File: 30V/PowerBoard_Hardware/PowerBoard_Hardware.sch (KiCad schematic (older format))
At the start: 141 parts, among them Q1 Q_NMOS_GDS, Q10 Q_NMOS_GDS, Q2 Q_NMOS_GDS, Q3 Q_NMOS_GDS, Q4 Q_NMOS_GDS, Q5 Q_NMOS_GDS, Q6 Q_NMOS_GDS, Q7 Q_NMOS_GDS, Q8 Q_NMOS_GDS, Q9 Q_NMOS_GDS, U1 LT1910, U10 LT1910, U11 LT1910, U12 ACS722xLCTR-40AU, U13 ACS722xLCTR-40AU, U14 ACS722xLCTR-40AU, U15 OKI_5V, U16 OKI_3V3, U17 LT1910, U18 LT1910, U19 ACS722xLCTR-40AU, U2 LT1910, U20 ACS722xLCTR-40AU, U21 LT1910, U22 ACS722xLCTR-40AU, U3 LT1910, U4 LT1910, U5 ACS722xLCTR-40AU, U6 ACS722xLCTR-40AU, U7 ACS722xLCTR-40AU, U8 ACS722xLCTR-40AU, U9 LT1910

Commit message: redid PVDD
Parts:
- ConnTIVA_L1, ConnTIVA_R1: footprint Connector_PinHeader_1.27mm:PinHeader_2x05_P1.27mm_Vertical -> MRDT_Connectors:JTAG_ARM_Connector_10_Pin
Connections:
- net GND: now also C22.2, C25.2, C26.2, C27.2, D1.2 (A), D2.2 (A)
- net PVDD: now also C22.1, C25.1, C26.1, C27.1, D1.1 (K), D2.1 (K), V1.1; no longer C22.2, C25.2, C26.2, C27.2, D1.2 (A), D2.2 (A)
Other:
- note added: "12V_Board"
- moved on the sheet: C22, C25, C26, C27, D1, D2
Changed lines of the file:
@@
 Wire Wire Line
 	5450 5150 5450 5300
-Text GLabel 2700 4350 2    50   Output ~ 0
+Text GLabel 2700 3950 1    50   Output ~ 0
 PVDD
 Text GLabel 4750 850  0    50   Input ~ 0
@@
 F 0 "ConnTIVA_L1" H 1550 1550 60  0000 L CNN
 F 1 "PH_2x05" H 1650 1450 60  0000 L CNN
-F 2 "Connector_PinHeader_1.27mm:PinHeader_2x05_P1.27mm_Vertical" H 1800 1400 60  0001 C CNN
+F 2 "MRDT_Connectors:JTAG_ARM_Connector_10_Pin" H 1800 1400 60  0001 C CNN
 F 3 "" H 1800 1400 60  0001 C CNN
 	1    1800 1100
@@
 U 1 1 5E0EEBAD
 P 1700 2950
-F 0 "ConnTIVA_PWR1" H 1828 3208 60  0000 L CNN
+F 0 "ConnTIVA_PWR1" H 1850 3000 60  0000 L CNN
 F 1 "Molex_SL_02" H 1828 3102 60  0000 L CNN
 F 2 "MRDT_Connectors:MOLEX_SL_02_Vertical" H 1700 2950 60  0001 C CNN
@@
 L Device:CP1_Small C22
 U 1 1 5E7C9F9E
-P 750 4250
-F 0 "C22" H 838 4296 50  0000 L CNN
-F 1 "470uF" H 838 4205 50  0000 L CNN
-F 2 "Capacitor_THT:CP_Radial_D12.5mm_P5.00mm" H 750 4250 50  0001 C CNN
-F 3 "~" H 750 4250 50  0001 C CNN
-	1    750  4250
+P 750 4150
+F 0 "C22" H 838 4196 50  0000 L CNN
+F 1 "470uF" H 838 4105 50  0000 L CNN
+F 2 "Capacitor_THT:CP_Radial_D12.5mm_P5.00mm" H 750 4150 50  0001 C CNN
+F 3 "~" H 750 4150 50  0001 C CNN
+	1    750  4150
 	1    0    0    -1
 $EndComp
@@
 L Device:CP1_Small C25
 U 1 1 5E808371
-P 1100 4250
-F 0 "C25" H 1188 4296 50  0000 L CNN
-F 1 "470uF" H 1188 4205 50  0000 L CNN
-F 2 "Capacitor_THT:CP_Radial_D12.5mm_P5.00mm" H 1100 4250 50  0001 C CNN
-F 3 "~" H 1100 4250 50  0001 C CNN
-	1    1100 4250
+P 1100 4150
+F 0 "C25" H 1188 4196 50  0000 L CNN
+F 1 "470uF" H 1188 4105 50  0000 L CNN
+F 2 "Capacitor_THT:CP_Radial_D12.5mm_P5.00mm" H 1100 4150 50  0001 C CNN
+F 3 "~" H 1100 4150 50  0001 C CNN
+	1    1100 4150
 	1    0    0    -1
 $EndComp
@@
 L Device:CP1_Small C26
 U 1 1 5E808517
-P 1450 4250
-F 0 "C26" H 1538 4296 50  0000 L CNN
-F 1 "470uF" H 1538 4205 50  0000 L CNN
-F 2 "Capacitor_THT:CP_Radial_D12.5mm_P5.00mm" H 1450 4250 50  0001 C CNN
-F 3 "~" H 1450 4250 50  0001 C CNN
-	1    1450 4250
+P 1450 4150
+F 0 "C26" H 1538 4196 50  0000 L CNN
+F 1 "470uF" H 1538 4105 50  0000 L CNN
+F 2 "Capacitor_THT:CP_Radial_D12.5mm_P5.00mm" H 1450 4150 50  0001 C CNN
+F 3 "~" H 1450 4150 50  0001 C CNN
+	1    1450 4150
 	1    0    0    -1
 $EndComp
@@
 L Device:CP1_Small C27
 U 1 1 5E808A8A
-P 1800 4250
-F 0 "C27" H 1888 4296 50  0000 L CNN
-F 1 "470uF" H 1888 4205 50  0000 L CNN
-F 2 "Capacitor_THT:CP_Radial_D12.5mm_P5.00mm" H 1800 4250 50  0001 C CNN
-F 3 "~" H 1800 4250 50  0001 C CNN
-	1    1800 4250
-	1    0    0    -1
-$EndComp
-Wire Wire Line
-	750  4350 1100 4350
-Connection ~ 1100 4350
-Wire Wire Line
-	1100 4350 1450 4350
-Connection ~ 1450 4350
-Wire Wire Line
-	1450 4350 1800 4350
-Connection ~ 1800 4350
-Wire Wire Line
-	1800 4350 2100 4350
+P 1800 4150
+F 0 "C27" H 1888 4196 50  0000 L CNN
+F 1 "470uF" H 1888 4105 50  0000 L CNN
+F 2 "Capacitor_THT:CP_Radial_D12.5mm_P5.00mm" H 1800 4150 50  0001 C CNN
+F 3 "~" H 1800 4150 50  0001 C CNN
+	1    1800 4150
+	1    0    0    -1
+$EndComp
 $Comp
 L Device:D D1
 U 1 1 5E901D4D
-P 2100 4200
-F 0 "D1" V 2054 4279 50  0000 L CNN
-F 1 "1.5KE36A" V 2145 4279 50  0000 L CNN
-F 2 "Diode_THT:D_DO-201AD_P5.08mm_Vertical_KathodeUp" H 2100 4200 50  0001 C CNN
-F 3 "~" H 2100 4200 50  0001 C CNN
-	1    2100 4200
+P 2100 4150
+F 0 "D1" V 2054 4229 50  0000 L CNN
+F 1 "1.5KE36A" V 2145 4229 50  0000 L CNN
+F 2 "Diode_THT:D_DO-201AD_P5.08mm_Vertical_KathodeUp" H 2100 4150 50  0001 C CNN
+F 3 "~" H 2100 4150 50  0001 C CNN
+	1    2100 4150
 	0    1    1    0
 $EndComp
 Wire Wire Line
-	2600 4050 2600 4000
-Wire Wire Line
 	650  4000 750  4000
-Wire Wire Line
-	2100 4050 2100 4000
-Wire Wire Line
-	1800 4150 1800 4000
-Connection ~ 1800 4000
-Wire Wire Line
-	1800 4000 2100 4000
-Wire Wire Line
-	1450 4150 1450 4000
 Connection ~ 1450 4000
-Wire Wire Line
-	1450 4000 1800 4000
-Wire Wire Line
-	1100 4150 1100 4000
-Connection ~ 1100 4000
-Wire Wire Line
-	1100 4000 1450 4000
-Wire Wire Line
-	750  4150 750  4000
 Connection ~ 750  4000
-Wire Wire Line
-	750  4000 1100 4000
 $Comp
 L Device:D D2
 U 1 1 5EA68DC6
-P 2600 4200
-F 0 "D2" V 2554 4279 50  0000 L CNN
-F 1 "1.5KE36A" V 2645 4279 50  0000 L CNN
-F 2 "Diode_THT:D_DO-201AD_P5.08mm_Vertical_KathodeUp" H 2600 4200 50  0001 C CNN
-F 3 "~" H 2600 4200 50  0001 C CNN
-	1    2600 4200
+P 2600 4150
+F 0 "D2" V 2554 4229 50  0000 L CNN
+F 1 "1.5KE36A" V 2645 4229 50  0000 L CNN
+F 2 "Diode_THT:D_DO-201AD_P5.08mm_Vertical_KathodeUp" H 2600 4150 50  0001 C CNN
+F 3 "~" H 2600 4150 50  0001 C CNN
+	1    2600 4150
 	0    1    1    0
 $EndComp
-Connection ~ 2600 4350
-Wire Wire Line
-	2600 4350 2700 4350
+Connection ~ 2600 4300
+Wire Wire Line
+	2600 4300 2700 4300
 $Comp
 L MRDT_Connectors:AndersonPP Conn1
@@
 Wire Wire Line
 	9600 10150 9650 10150
-Text Notes 8100 10200 0    118  ~ 0
-12V
+Text Notes 7600 10200 0    118  ~ 0
+12V_Board
 Wire Wire Line
 	8950 10150 8900 10150
@@
 $EndComp
 Wire Wire Line
-	2100 4350 2600 4350
-Connection ~ 2100 4350
+	2100 4300 2600 4300
+Connection ~ 2100 4300
 Wire Wire Line
 	2100 4000 2600 4000
@@
 F 0 "ConnTIVA_R1" H 1850 2450 60  0000 C CNN
 F 1 "PH_2x05" H 1850 2550 60  0000 C CNN
-F 2 "Connector_PinHeader_1.27mm:PinHeader_2x05_P1.27mm_Vertical" H 1800 2450 60  0001 C CNN
+F 2 "MRDT_Connectors:JTAG_ARM_Connector_10_Pin" H 1800 2450 60  0001 C CNN
 F 3 "" H 1800 2450 60  0001 C CNN
 	1    1800 2150
@@
 Wire Notes Line
 	450  450  12050 450
+Wire Wire Line
+	1450 4050 1450 4000
+Wire Wire Line
+	750  4050 750  4000
+Wire Wire Line
+	750  4300 1100 4300
+Wire Wire Line
+	1800 4250 1800 4300
+Connection ~ 1800 4300
+Wire Wire Line
+	1800 4300 2100 4300
+Wire Wire Line
+	1450 4250 1450 4300
+Connection ~ 1450 4300
+Wire Wire Line
+	1450 4300 1800 4300
+Wire Wire Line
+	1100 4250 1100 4300
+Connection ~ 1100 4300
+Wire Wire Line
+	1100 4300 1450 4300
+Wire Wire Line
+	750  4250 750  4300
+Wire Wire Line
+	750  4000 1100 4000
+Wire Wire Line
+	1450 4000 1800 4000
+Wire Wire Line
+	1800 4050 1800 4000
+Connection ~ 1800 4000
+Wire Wire Line
+	1800 4000 2100 4000
+Wire Wire Line
+	1100 4050 1100 4000
+Connection ~ 1100 4000
+Wire Wire Line
+	1100 4000 1450 4000
+Wire Wire Line
+	2600 4000 2700 4000
+Connection ~ 2600 4000
+$Comp
+L power:GND #PWR?
+U 1 1 5E180990
+P 2700 4300
+F 0 "#PWR?" H 2700 4050 50  0001 C CNN
+F 1 "GND" H 2705 4127 50  0000 C CNN
+F 2 "" H 2700 4300 50  0001 C CNN
+F 3 "" H 2700 4300 50  0001 C CNN
+	1    2700 4300
+	1    0    0    -1
+$EndComp
+Wire Wire Line
+	2700 3950 2700 4000
 $EndSCHEMATC

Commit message: fixed schematic b/c Zac made fun of me
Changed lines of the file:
@@
 Text Notes 3200 9650 0    118  ~ 0
 +5V
-Text Notes 5050 9250 0    118  ~ 0
+Text Notes 5150 9300 0    118  ~ 0
 Motor1
-Text Notes 5050 9700 0    118  ~ 0
+Text Notes 5100 9750 0    118  ~ 0
 Motor2
 Wire Wire Line
@@
 Wire Wire Line
 	6800 10150 6850 10150
-Text Notes 5050 10150 0    118  ~ 0
+Text Notes 5100 10200 0    118  ~ 0
 Motor3
 Wire Wire Line
@@
 Wire Wire Line
 	6800 10550 6850 10550
-Text Notes 5050 10550 0    118  ~ 0
+Text Notes 5100 10600 0    118  ~ 0
 Motor4
 Wire Wire Line
@@
 Wire Wire Line
 	6800 11000 6850 11000
-Text Notes 5050 11000 0    118  ~ 0
+Text Notes 5100 11050 0    118  ~ 0
 Motor5
 Wire Wire Line
@@
 Wire Wire Line
 	9600 9700 9650 9700
-Text Notes 7850 9250 0    118  ~ 0
+Text Notes 7800 9300 0    118  ~ 0
 Rockets
-Text Notes 7800 9700 0    118  ~ 0
+Text Notes 7750 9750 0    118  ~ 0
 Auxiliary
 Wire Wire Line
@@
 Wire Wire Line
 	9600 10550 9650 10550
-Text Notes 7900 10550 0    118  ~ 0
+Text Notes 8050 10600 0    118  ~ 0
 Spare
 Wire Wire Line
@@
 Wire Wire Line
 	9600 11000 9650 11000
-Text Notes 7850 11000 0    118  ~ 0
+Text Notes 7950 11050 0    118  ~ 0
 Motor6
 Wire Wire Line
@@
 Connection ~ 2600 4000
 $Comp
-L power:GND #PWR?
+L power:GND #PWR0143
 U 1 1 5E180990
 P 2700 4300
-F 0 "#PWR?" H 2700 4050 50  0001 C CNN
+F 0 "#PWR0143" H 2700 4050 50  0001 C CNN
 F 1 "GND" H 2705 4127 50  0000 C CNN
 F 2 "" H 2700 4300 50  0001 C CNN

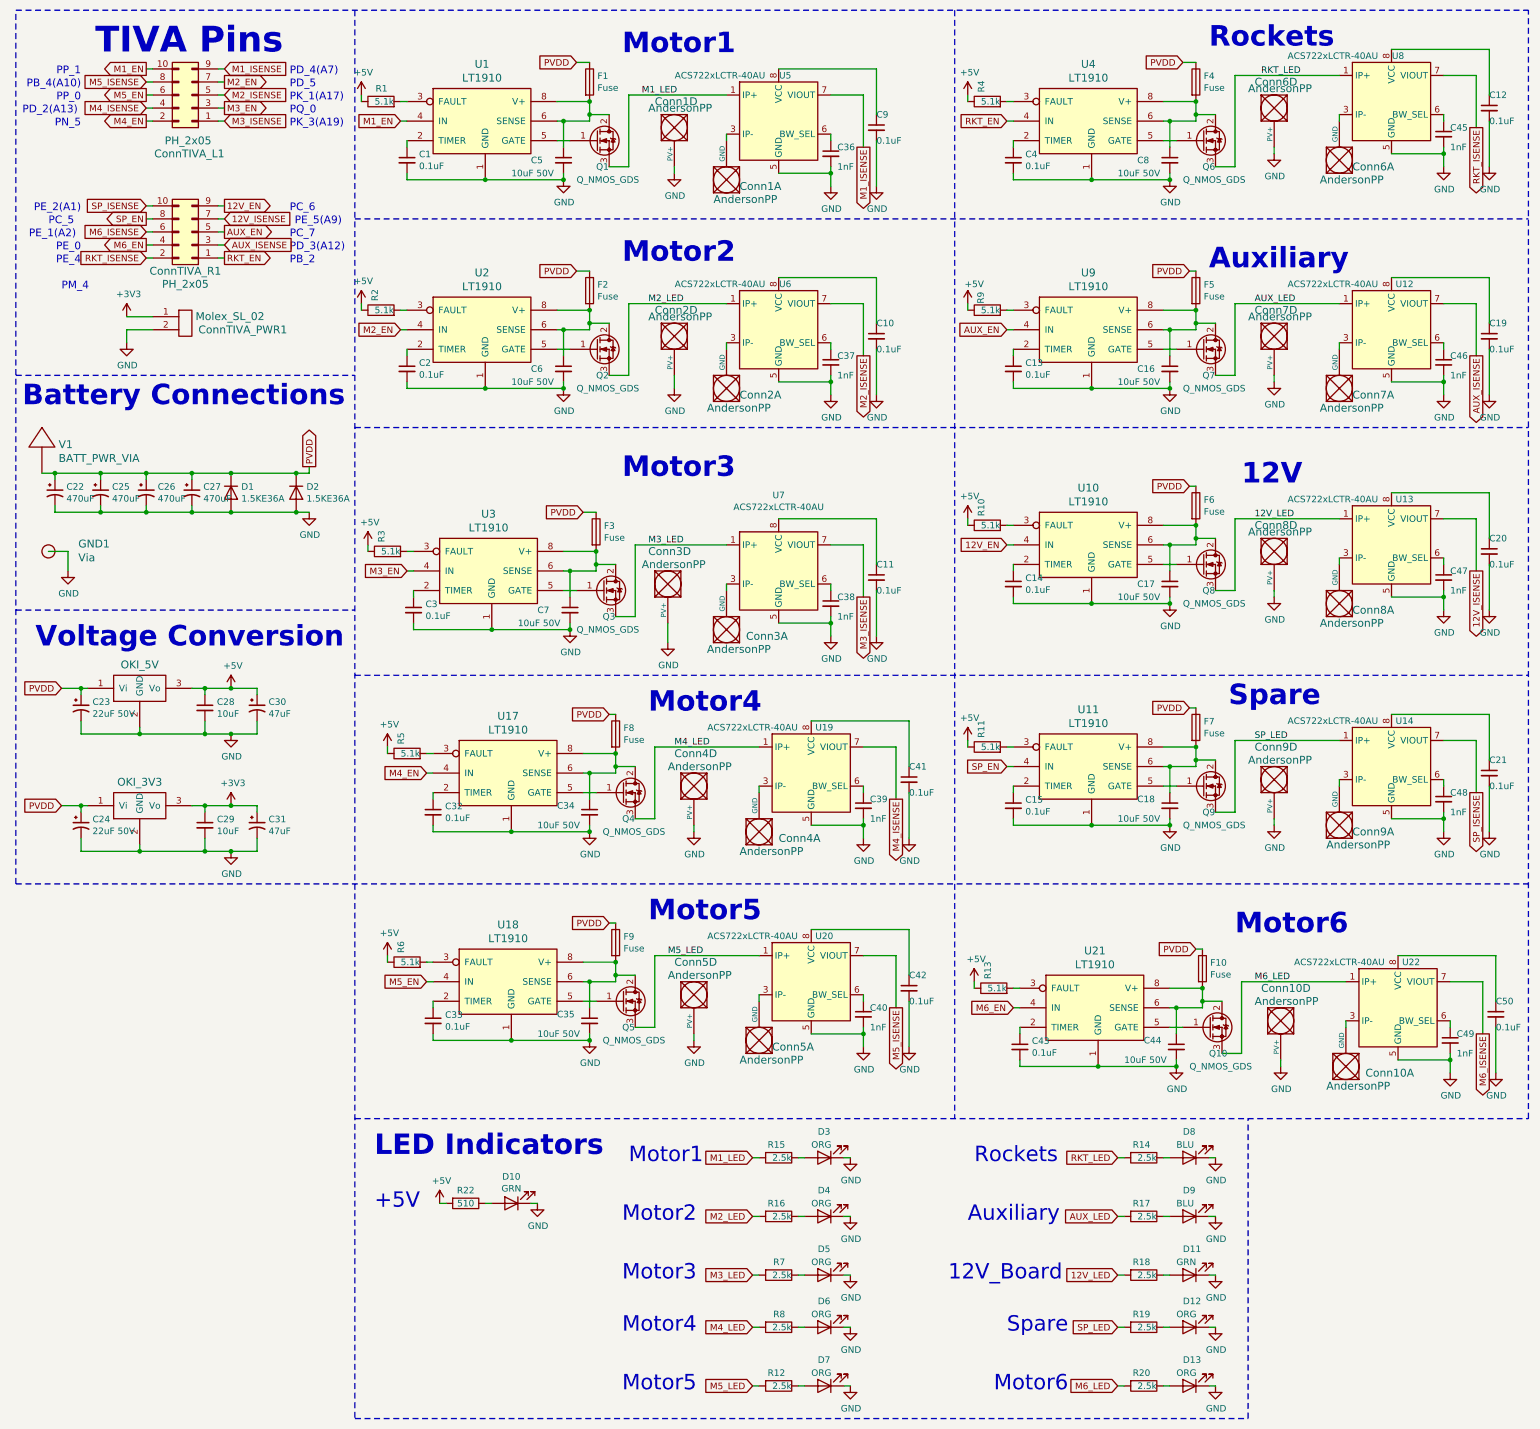
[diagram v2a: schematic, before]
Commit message: Left side current sensors have 3.3V
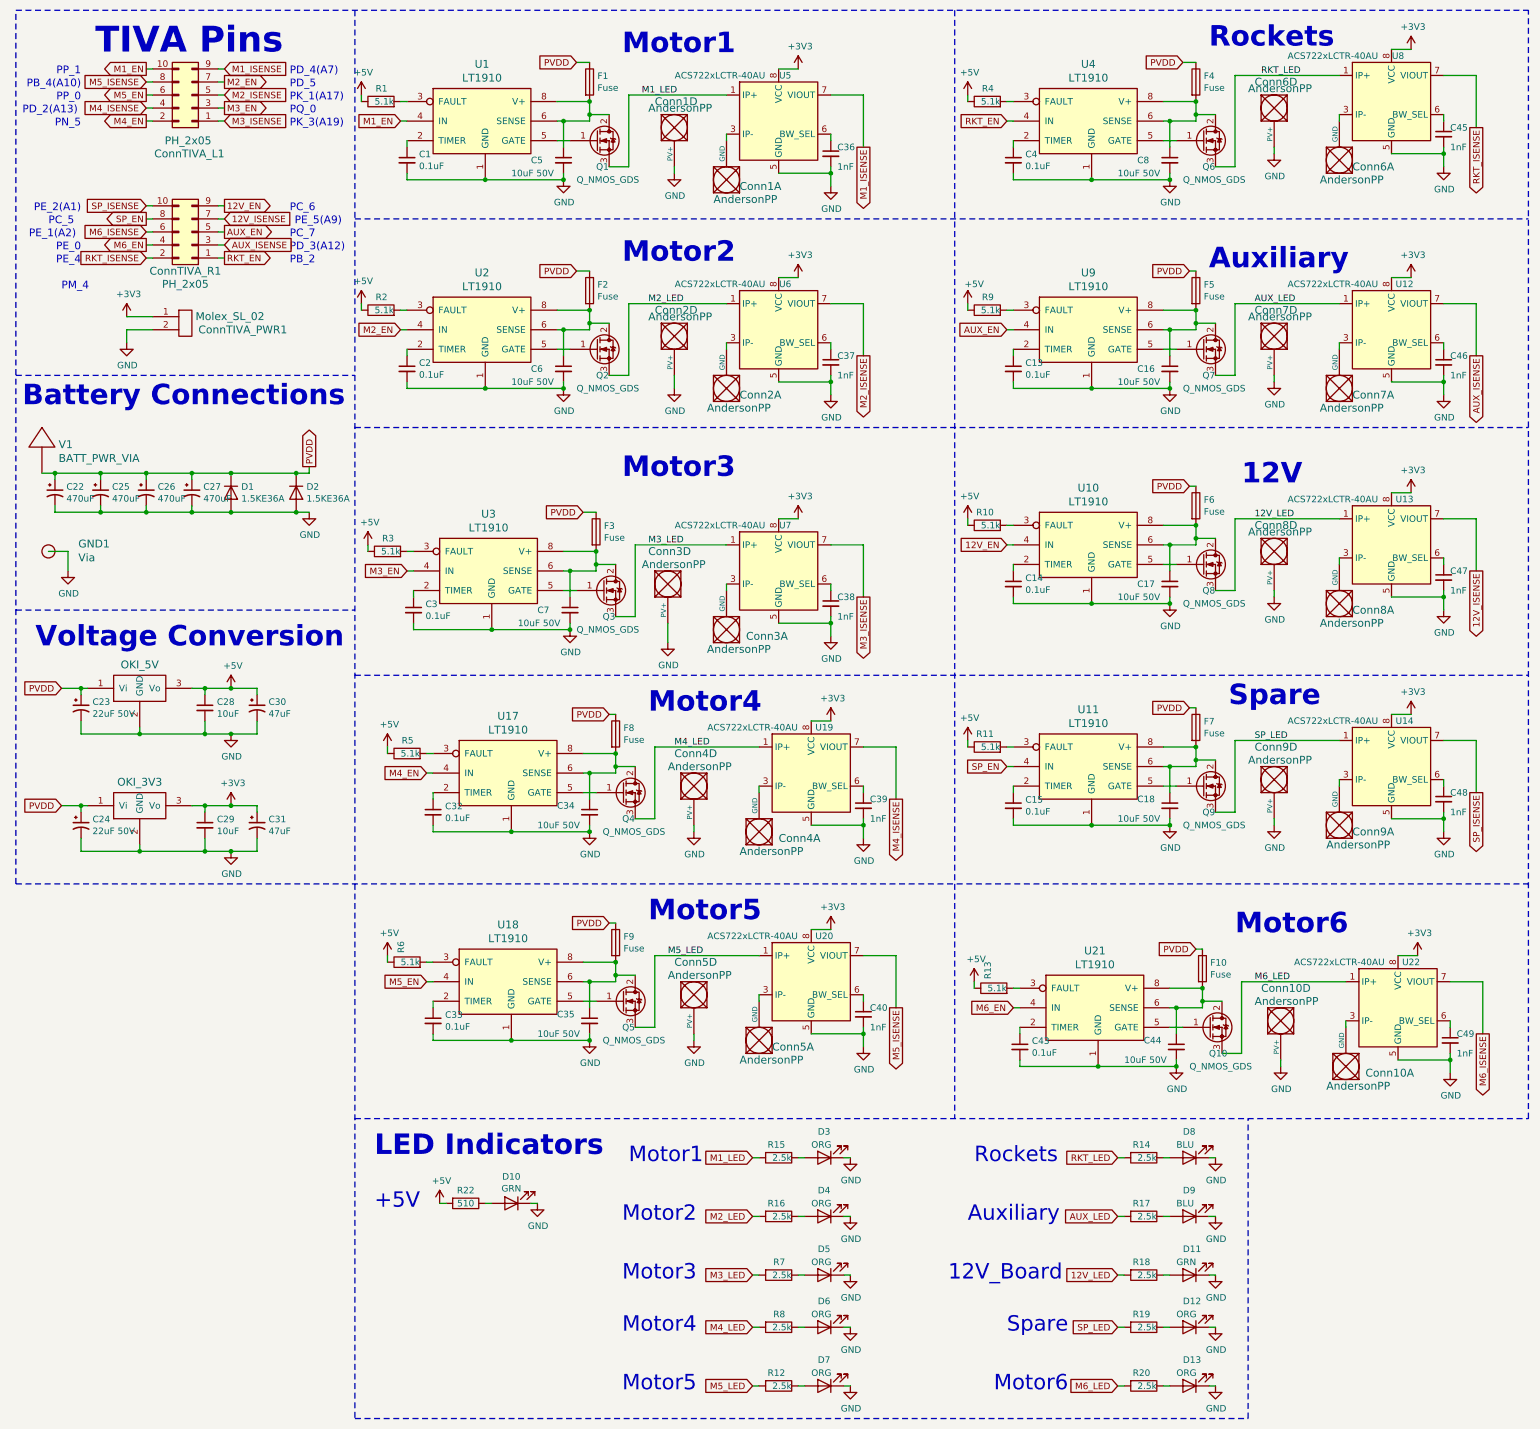
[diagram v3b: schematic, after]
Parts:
- removed C10, C11, C12, C19, C20, C21, C41, C42, C50, C9: 0.1uF, Capacitor_SMD:C_0603_1608Metric_Pad1.05x0.95mm_HandSolder, symbol Device:C_Small
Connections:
- net +3V3: now also U12.8 (VCC), U13.8 (VCC), U14.8 (VCC), U19.8 (VCC), U20.8 (VCC), U22.8 (VCC), U5.8 (VCC), U6.8 (VCC), U7.8 (VCC), U8.8 (VCC)
